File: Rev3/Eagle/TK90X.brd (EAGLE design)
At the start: 217.8 x 132.1 mm, 217 parts, among them IC1 Z80, IC10 74LS365N, IC11 LM1886, IC12 LM1889, IC13 4116, IC14 4116, IC15 4116, IC16 4116, IC17 4116, IC18 4116, IC19 4116, IC2 ROM, IC20 4116, IC21 4416, IC22 4416, IC23 4416, IC24 4416, IC25 74LS00, IC26 74LS00, IC27 74LS32, IC28 74LS04, IC3 ULA TK90, IC4 74LS74, IC5 74LS74, IC6 74LS157, IC7 74LS157, IC8 74LS157, IC9 74LS157, Q1 BC548, Q2 BC548, Q3 BF494, Q4 BC548, Q5 BD139, Q6 BD136, Q7 BC548, X2 POWER

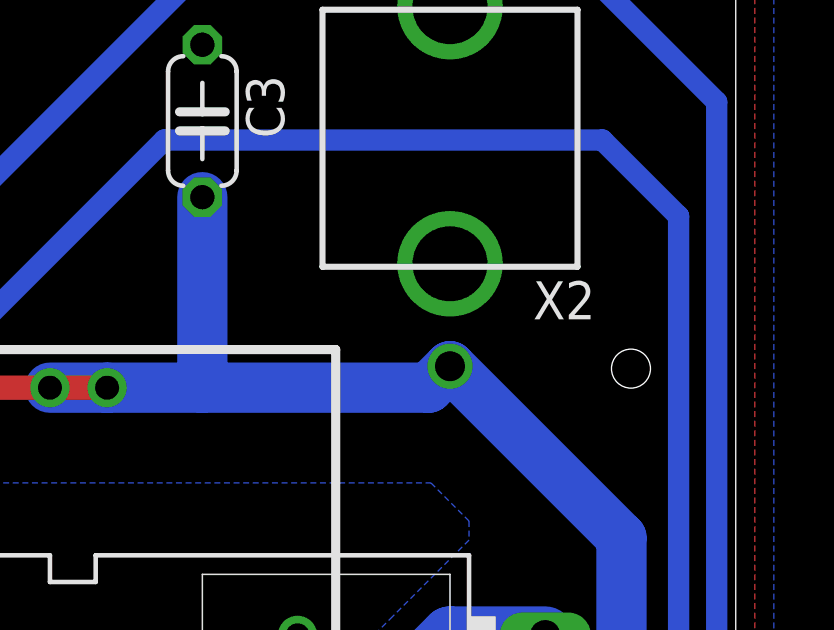
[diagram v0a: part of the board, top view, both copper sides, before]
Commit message: Corrigido conexões power Adicionado jumpers de solda pros jacks de áudio Adicionado revisão 6 com 74LS365 substituido pelo 74LS244
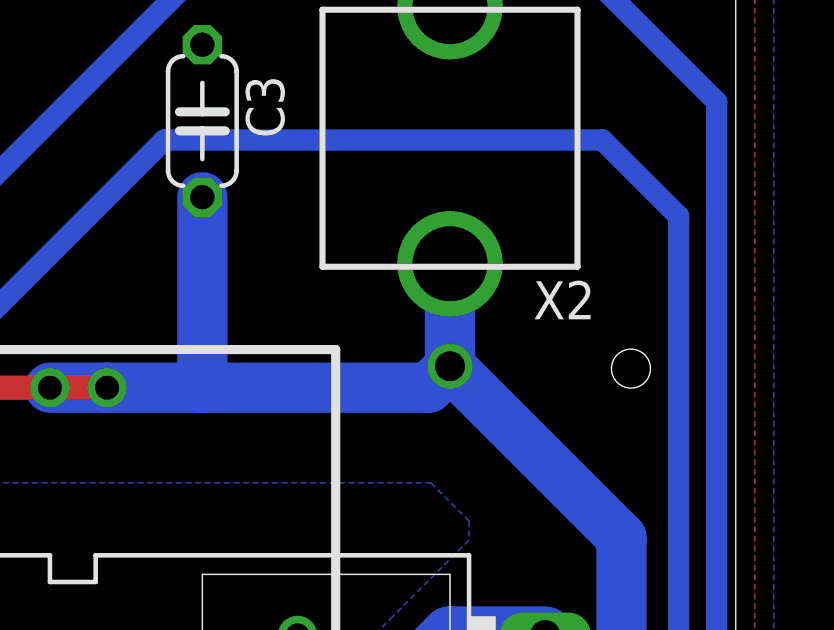
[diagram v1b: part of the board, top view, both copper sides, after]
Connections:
- net V+: now also X2.NC
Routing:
- net V+: track 520.4 -> 523.8 mm
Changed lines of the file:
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@@
 <layer number="25" name="tNames" color="7" fill="1" visible="yes" active="yes"/>
 <layer number="26" name="bNames" color="7" fill="1" visible="yes" active="yes"/>
-<layer number="27" name="tValues" color="7" fill="1" visible="no" active="yes"/>
+<layer number="27" name="tValues" color="9" fill="1" visible="no" active="yes"/>
 <layer number="28" name="bValues" color="7" fill="1" visible="no" active="yes"/>
 <layer number="29" name="tStop" color="7" fill="3" visible="no" active="yes"/>
@@
 <wire x1="200.025" y1="114.935" x2="207.565" y2="114.935" width="1.6764" layer="16"/>
 <wire x1="207.565" y1="114.935" x2="208.28" y2="115.65" width="1.6764" layer="16"/>
+<contactref element="X2" pad="NC"/>
+<wire x1="208.28" y1="115.65" x2="208.28" y2="119.065" width="1.6764" layer="16"/>
 </signal>
 </signals>
